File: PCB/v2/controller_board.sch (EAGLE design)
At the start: 58 parts, among them M1 B4B-PH-K-S(LF)(SN), M1_TMC TMC2209_SILENTSTEPSTICK, M2 B4B-PH-K-S(LF)(SN), M2_TMC TMC2209_SILENTSTEPSTICK, M3 B4B-PH-K-S(LF)(SN), M3_TMC TMC2209_SILENTSTEPSTICK, M4 B4B-PH-K-S(LF)(SN), M4_TMC TMC2209_SILENTSTEPSTICK

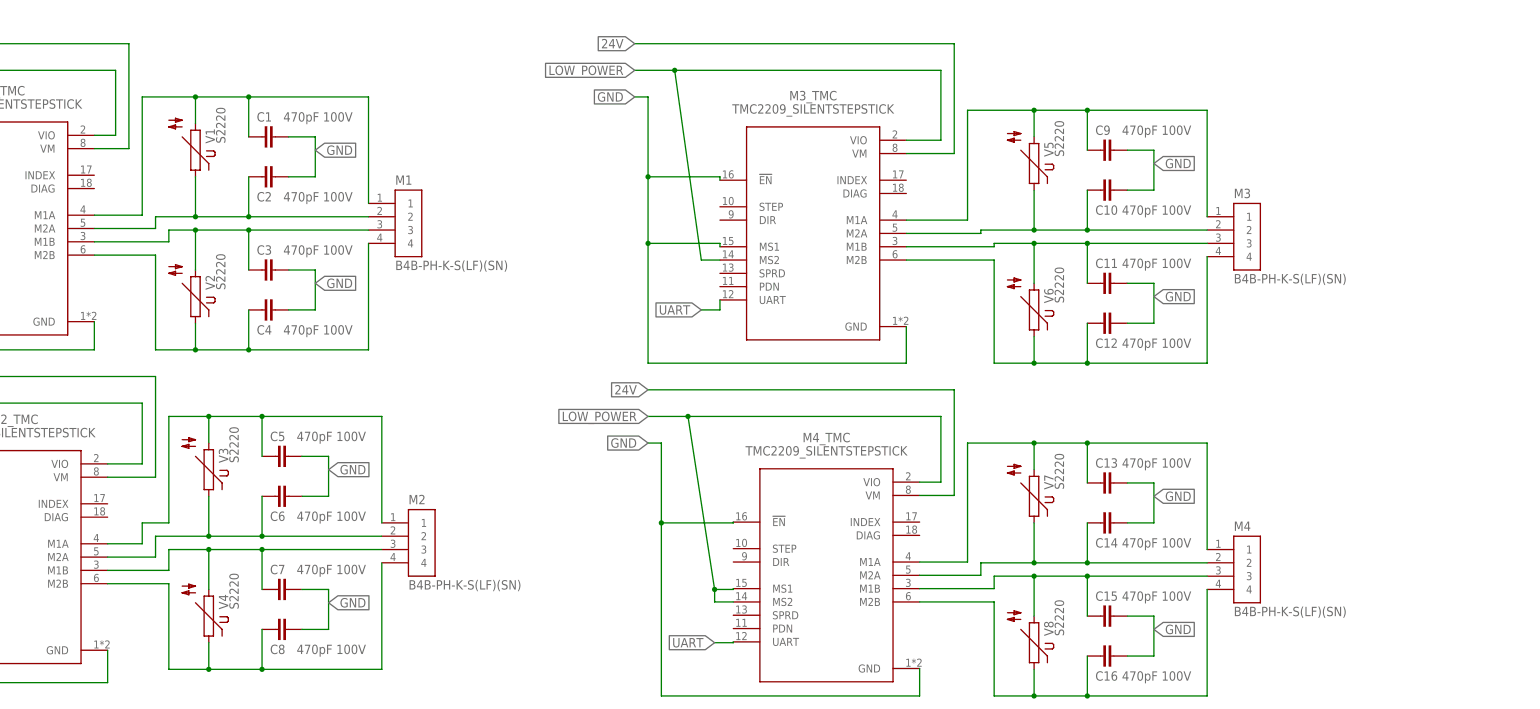
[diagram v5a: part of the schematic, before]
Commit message: feat(pcb): replace ESD protection with TVS-Diode
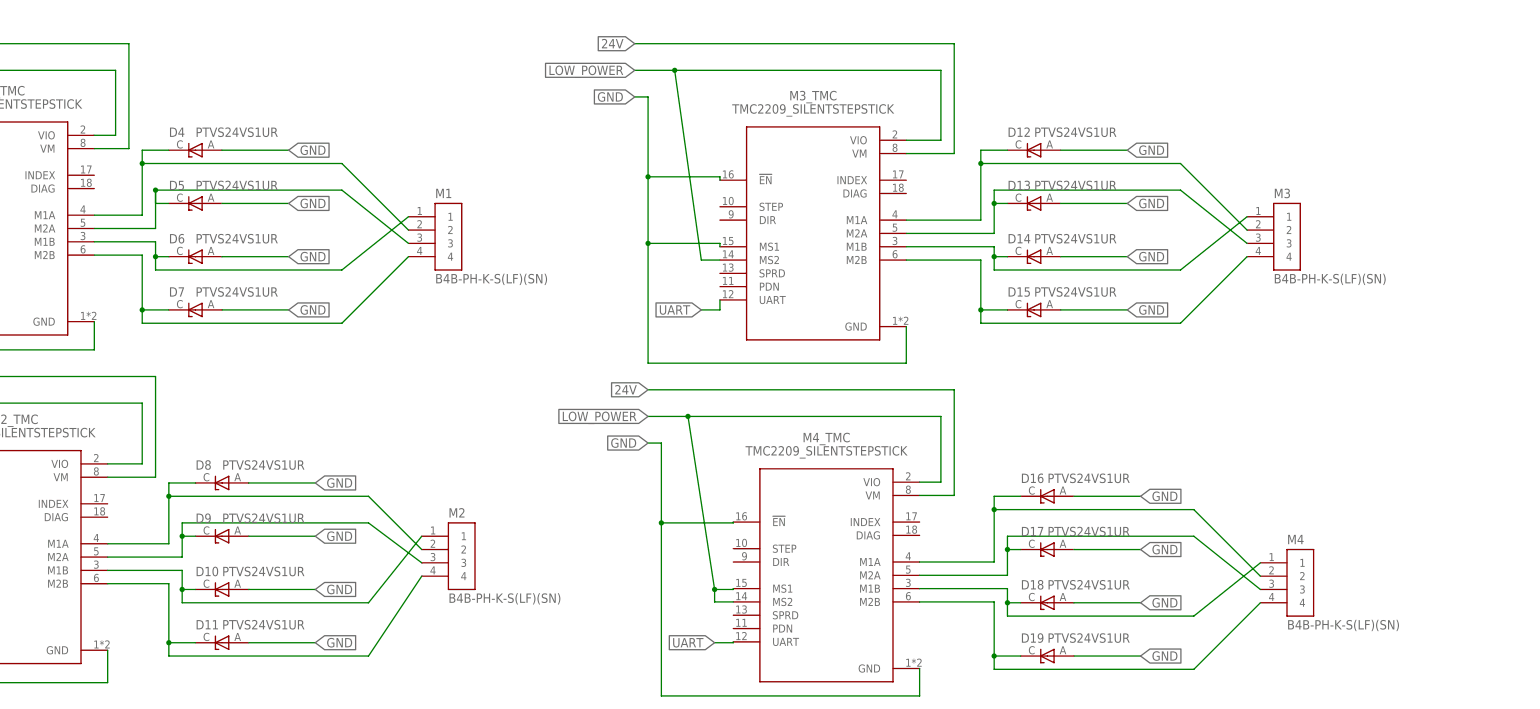
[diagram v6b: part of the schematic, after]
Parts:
- removed C1, C10, C11, C12, C13, C14, C15, C16, C2, C3, C4, C5, C6, C7, C8, C9: 470pF 100V, rcl:C-EUC0402
- removed V1, V2, V3, V4, V5, V6, V7, V8: S2220, varistor:S2220
- added D10, D11, D12, D13, D14, D15, D16, D17, D18, D19, D4, D5, D6, D7, D8, D9: PTVS24VS1UR, PTVS24VS1UR:PTVS24VS1UR
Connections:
- removed net N$22: C13.2, M4.1, M4_TMC.M1A, V7.2
- new net N$9: D12.C, M3.2, M3_TMC.M1A
- net GND: now also D10.A, D11.A, D12.A, D13.A, D14.A, D15.A, D16.A, D17.A, D18.A, D19.A, D4.A, D5.A, D6.A, D7.A, D8.A, D9.A; no longer C1.1, C10.1, C11.1, C12.1, C13.1, C14.1, C15.1, C16.1, C2.1, C3.1, C4.1, C5.1, C6.1, C7.1, C8.1, C9.1
- net N$10: now also D15.C; no longer C12.2, V6.1
- net N$11: now also D13.C, M3_TMC.M2A; no longer C11.2, M3_TMC.M1B, V6.2
- net N$12: now also D14.C, M3_TMC.M1B; no longer C9.2, M3_TMC.M1A, V5.2
- net N$13: now also D16.C, M4_TMC.M1A; no longer C14.2, M4_TMC.M2A, V7.1
- net N$14: now also D19.C, M4.4, M4_TMC.M2B; no longer C10.2, M3.2, M3_TMC.M2A, V5.1
- net N$15: now also D17.C, M4.3, M4_TMC.M2A; no longer C16.2, M4.4, M4_TMC.M2B, V8.1
- net N$16: now also D18.C, M4.1; no longer C15.2, M4.3, V8.2
- net N$19: now also D7.C, M1.4, M1_TMC.M2B; no longer C3.2, M1.3, M1_TMC.M1B, V2.2
- net N$2: now also D4.C, M1_TMC.M1A; no longer C2.2, M1_TMC.M2A, V1.1
- net N$26: now also D5.C, M1.3, M1_TMC.M2A; no longer C1.2, M1.1, M1_TMC.M1A, V1.2
- net N$4: now also D6.C, M1.1, M1_TMC.M1B; no longer C4.2, M1.4, M1_TMC.M2B, V2.1
- net N$5: now also D8.C, M2_TMC.M1A; no longer C6.2, M2_TMC.M2A, V3.1
- net N$6: now also D11.C; no longer C8.2, V4.1
- net N$7: now also D9.C, M2_TMC.M2A; no longer C7.2, M2_TMC.M1B, V4.2
- net N$8: now also D10.C, M2_TMC.M1B; no longer C5.2, M2_TMC.M1A, V3.2
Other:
- moved on the sheet: M1, M2, M3, M4

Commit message: feat(pcb): add TMC enable pin
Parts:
- removed I2C_1: B2B-PH-K-S(LF)(SN), B2B-PH-K-S_LF__SN_:B2B-PH-K-S(LF)(SN)
- added R11: 0R, rcl:R-EU_R0805
- renumbered SPI to SPI_I2C
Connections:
- removed net SCL: CONTROLLER.7, I2C_1.2
- removed net SDA: CONTROLLER.6, I2C_1.1
- new net 3V3: 3V3_FUSE1.2, D1.C, R11.2
- new net TMC_EN: CONTROLLER.7, M1_TMC.!EN, M2_TMC.!EN, M3_TMC.!EN, M4_TMC.!EN
- net GND: no longer M1_TMC.!EN, M2_TMC.!EN, M3_TMC.!EN, M4_TMC.!EN
- net LOW_POWER: now also R11.1; no longer 3V3_FUSE1.2, D1.C
